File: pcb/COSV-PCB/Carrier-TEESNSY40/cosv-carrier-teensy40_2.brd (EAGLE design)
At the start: 96.8 x 26.7 mm, 21 parts, among them K1 61200821621, K2 61200821621, K3 61200821621

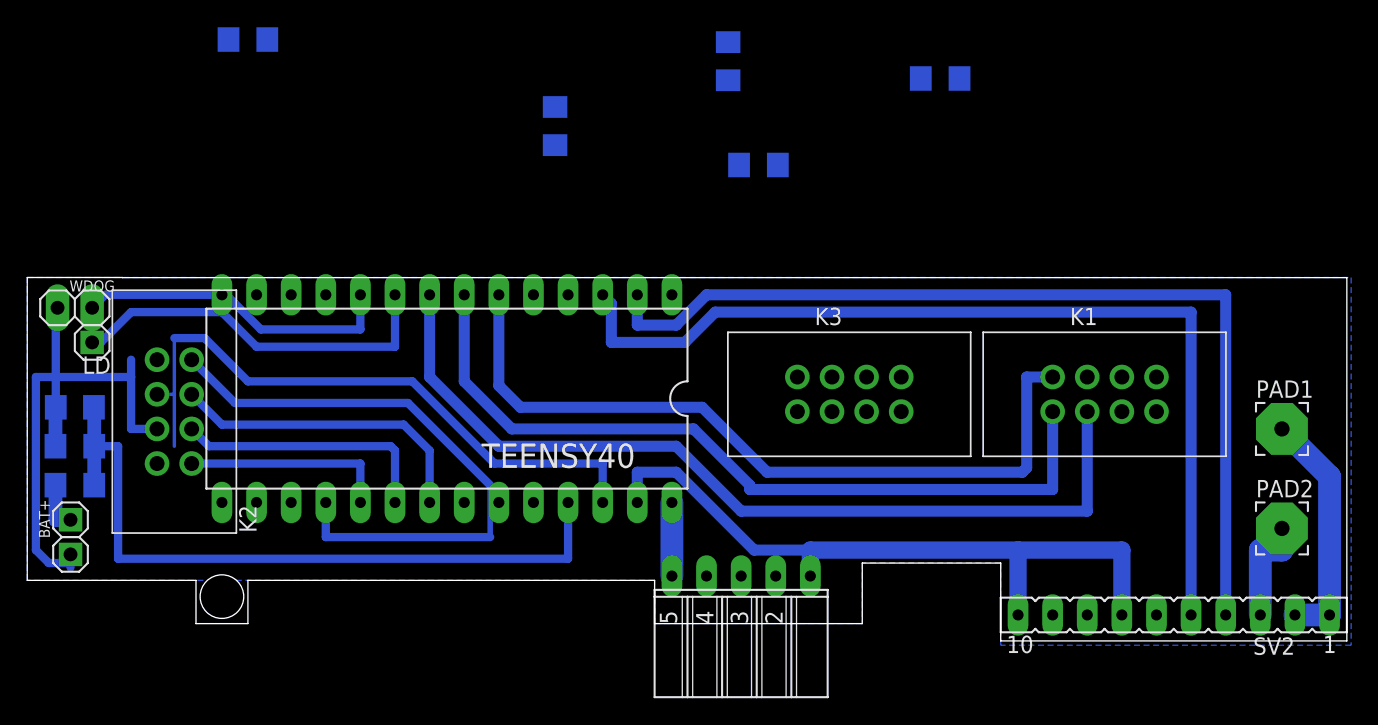
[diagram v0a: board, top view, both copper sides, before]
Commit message: Routed for easier milling
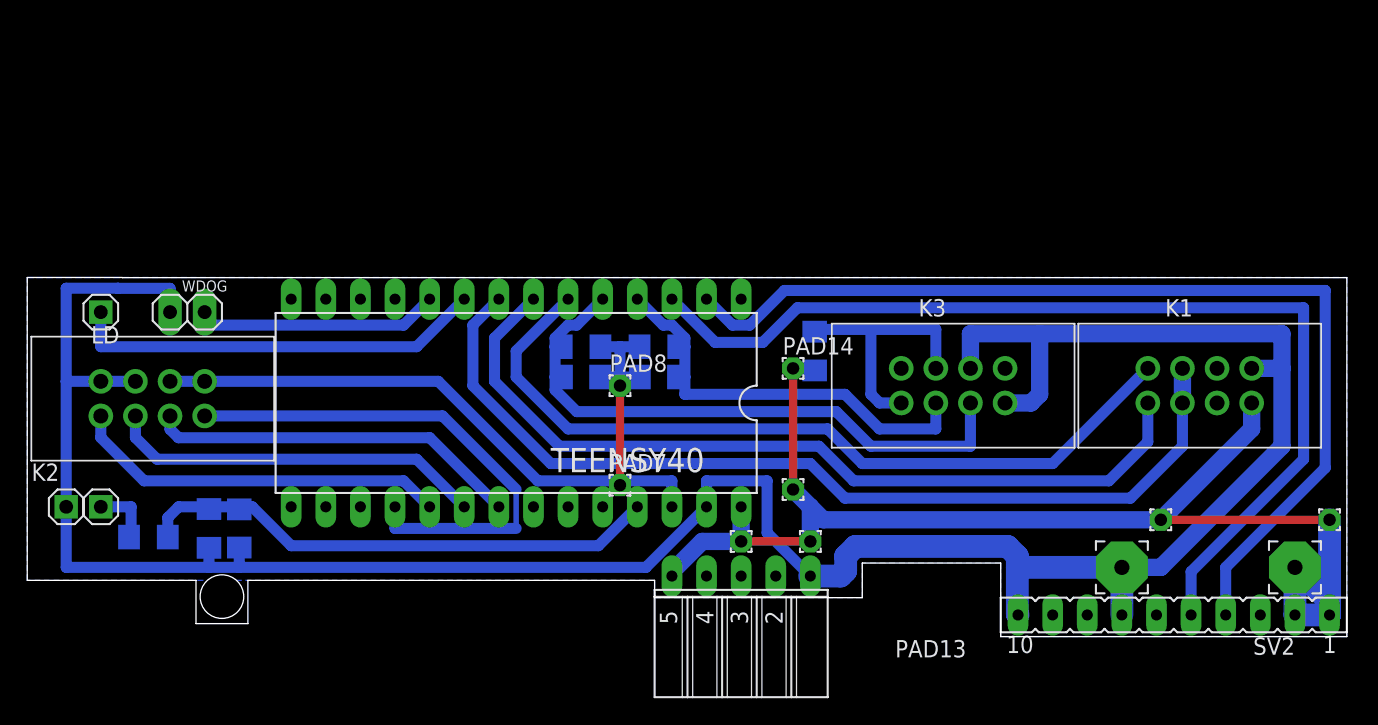
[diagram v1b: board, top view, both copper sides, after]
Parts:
- added PAD10, PAD11, PAD12, PAD13, PAD14, PAD7, PAD8, PAD9: (no value), wirepad:1,6/0,9
- moved R4 37.7 mm to (49.8, 23.2), turned to 0 degrees
- moved C3 25.6 mm to (44.1, 21.0), turned to 180 degrees
- moved R5 22.0 mm to (61.3, 22.9), turned to 270 degrees
- moved C2 19.9 mm to (49.8, 21.0), turned to 0 degrees
- moved R3 18.6 mm to (44.1, 23.2)
- moved C1 15.0 mm to (19.1, 9.84), turned to 270 degrees
- moved PAD2 12.1 mm to (83.8, 6.99)
- moved R2 11.5 mm to (16.8, 9.84), turned to 90 degrees
- moved PAD1 10.2 mm to (96.5, 6.99)
- moved WDOG 8.26 mm to (15.2, 25.7)
- moved K3 7.65 mm to (70.2, 20.3)
- moved K1 7.01 mm to (88.3, 20.3)
- moved GOLD_ORB_SM1 6.67 mm to (34.0, 19.1)
- moved R1 6.61 mm to (12.4, 9.21)
- moved TEENSY40 5.09 mm to (39.4, 19.1)
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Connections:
- net N$1 renamed LED
- net 3V3: now also C2.2, C3.2, PAD7.1, PAD8.1
- net GND: no longer C2.2, C3.2, SV2.3, TEENSY40.1
- net VCC: now also PAD10.1, PAD11.1, PAD12.1, PAD13.1, PAD14.1, PAD9.1
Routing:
- net GND: track 100.5 -> 192.8 mm
- net VCC: track 23.3 -> 96.5 mm
- net ENCODER: track 0.00 -> 44.8 mm
- net HOME: track 0.00 -> 31.2 mm
- net LED: track 0.00 -> 19.1 mm
- net A_BATTERY: track 53.3 -> 39.0 mm
- net SDA1: track 15.2 -> 27.8 mm
- net 3V3: track 47.3 -> 58.0 mm
- net SDA0: track 19.4 -> 27.8 mm
- net SCL1: track 44.1 -> 38.4 mm
- net PULSER: track 23.7 -> 18.3 mm
- net TX1: track 69.4 -> 74.7 mm
- net SCL0: track 23.0 -> 27.5 mm
- net RX1: track 69.8 -> 74.1 mm
- net PWM: track 65.7 -> 69.9 mm
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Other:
- board size 96.8 x 26.7 mm -> 96.8 x 26.4 mm
- board text removed: "LEN"
- board text removed: "PWM"
- board text removed: "REN"
- board text removed: "enc"
- board text removed: "home"
